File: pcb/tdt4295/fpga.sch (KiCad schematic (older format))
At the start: 40 parts, among them J301 FPGA__debug, U301 S25FL127SABMFV101, U302 NUP4114UCW1T2G, U303 XC7A100T-FTG256-tdt4295

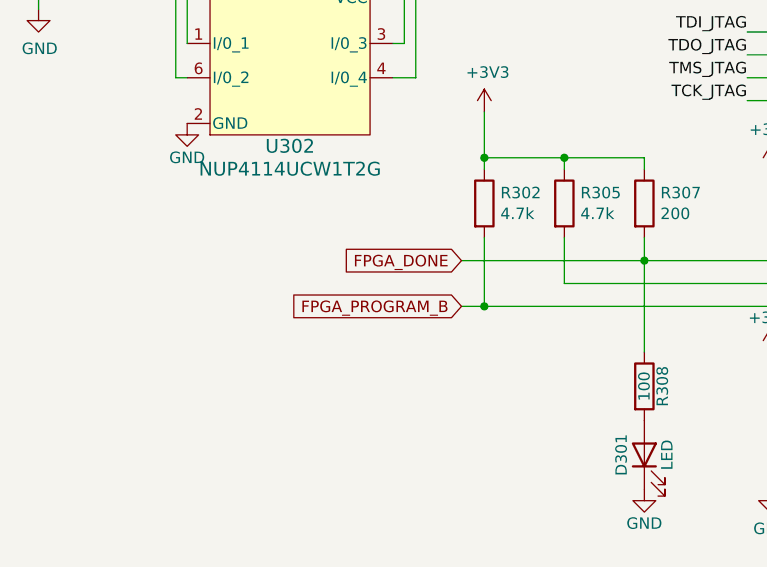
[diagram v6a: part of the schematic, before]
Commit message: footprints for everything
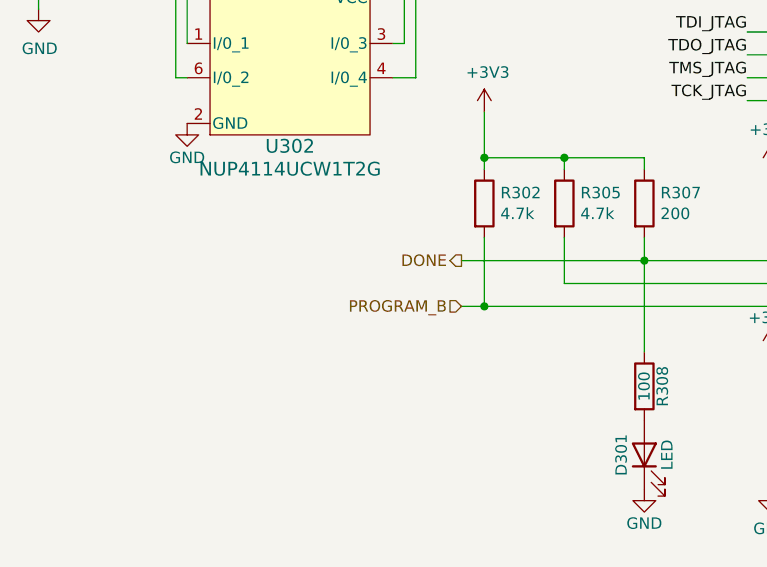
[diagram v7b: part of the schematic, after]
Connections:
- net FPGA_DONE renamed DONE
- net FPGA_PROGRAM_B renamed PROGRAM_B
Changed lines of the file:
@@
 	10900 2150 10900 2250
 Connection ~ 10900 2250
-Text GLabel 2400 6050 0    50   Input ~ 0
-FPGA_PROGRAM_B
 Wire Wire Line
 	3200 5850 2400 5850
@@
 	2500 6050 2400 6050
 Connection ~ 2500 6050
-Text GLabel 2400 5850 0    50   Input ~ 0
-FPGA_DONE
 Wire Wire Line
 	6600 6100 6600 5900
@@
 Connection ~ 6600 6100
 Connection ~ 6600 6400
+Text HLabel 2400 5850 0    50   Output ~ 0
+DONE
+Text HLabel 2400 6050 0    50   Input ~ 0
+PROGRAM_B
 $EndSCHEMATC

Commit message: associate component links with (almost) every component
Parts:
- D301: footprint Diode_SMD:D_0805_2012Metric_Pad1.15x1.40mm_HandSolder -> LED_SMD:LED_1206_3216Metric_Pad1.42x1.75mm_HandSolder; Component name (none) -> QTLP650C4TR; DK_Detail_Page (none) -> https://www.digikey.no/product-detail/no/everlight-electron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
- J301: footprint Connector_PinHeader_2.54mm:PinHeader_2x07_P2.54mm_Vertical -> Connector_PinHeader_2.54mm:PinHeader_2x07_P2.54mm_Vertical_SMD; Component name (none) -> 61001421121; DK_Detail_Page (none) -> https://www.digikey.no/product-detail/en/w%C3%BCrth-elektro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
- U301: Component name (none) -> S25FL127SABMFV101; DK_Detail_Page (none) -> https://no.farnell.com/cypress-semiconductor/s25fl127sabmfv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
- U302: footprint SOIC_W1T2G_ONS -> NUP4114UCW1T2G-footprint:NUP4114UCW1T2G
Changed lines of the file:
@@
 F 0 "D301" H 3200 6800 50  0000 C CNN
 F 1 "LED" H 3200 6600 50  0000 C CNN
-F 2 "Diode_SMD:D_0805_2012Metric_Pad1.15x1.40mm_HandSolder" H 3200 6700 50  0001 C CNN
+F 2 "LED_SMD:LED_1206_3216Metric_Pad1.42x1.75mm_HandSolder" H 3200 6700 50  0001 C CNN
 F 3 "~" H 3200 6700 50  0001 C CNN
+F 4 "QTLP650C4TR" H 3200 6700 50  0001 C CNN "Component name"
+F 5 "https://www.digikey.no/product-detail/no/everlight-electronics-co-ltd/QTLP650C4TR/1080-1415-1-ND/2676149" H 3200 6700 50  0001 C CNN "DK_Detail_Page"
 	1    3200 6700
 	0    -1   -1   0
@@
 F 2 "S25FL127SABMFV101-footprint:S25FL127SABMFV101" H 2250 2440 60  0001 C CNN
 F 3 "https://www.cypress.com/file/177961/download" H 750 2200 60  0001 C CNN
+F 4 "S25FL127SABMFV101" H 750 2200 50  0001 C CNN "Component name"
+F 5 "https://no.farnell.com/cypress-semiconductor/s25fl127sabmfv101/flash-memory-128mbit-108mhz-soic/dp/2772749?ost=s25fl127sabmfv101" H 750 2200 50  0001 C CNN "DK_Detail_Page"
 	1    750  2200
 	1    0    0    -1
@@
 F 0 "J301" H 800 4767 50  0000 C CNN
 F 1 "FPGA__debug" H 800 4676 50  0000 C CNN
-F 2 "Connector_PinHeader_2.54mm:PinHeader_2x07_P2.54mm_Vertical" H 750 4250 50  0001 C CNN
+F 2 "Connector_PinHeader_2.54mm:PinHeader_2x07_P2.54mm_Vertical_SMD" H 750 4250 50  0001 C CNN
 F 3 "~" H 750 4250 50  0001 C CNN
+F 4 "61001421121" H 750 4250 50  0001 C CNN "Component name"
+F 5 "https://www.digikey.no/product-detail/en/w%C3%BCrth-elektronik/61001421121/732-5465-5-ND/4846970" H 750 4250 50  0001 C CNN "DK_Detail_Page"
 	1    750  4250
 	1    0    0    -1
@@
 F 0 "U302" H 1650 4750 60  0000 C CNN
 F 1 "NUP4114UCW1T2G" H 1650 4650 60  0000 C CNN
-F 2 "SOIC_W1T2G_ONS" H 1650 4540 60  0001 C CNN
+F 2 "NUP4114UCW1T2G-footprint:NUP4114UCW1T2G" H 1650 4540 60  0001 C CNN
 F 3 "" H 850 3600 60  0000 C CNN
 	1    1650 5050
